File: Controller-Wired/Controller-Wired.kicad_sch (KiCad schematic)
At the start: 32 parts, among them J1 Conn_01x03, J2 Conn_02x20_Odd_Even, J3 Conn_01x06, J4 USB_C_Receptacle, SW1 SW_Push, U1 STM32F103CBTx, U2 AP131-33, U3 USBLC6-2SC6, Y1 Crystal

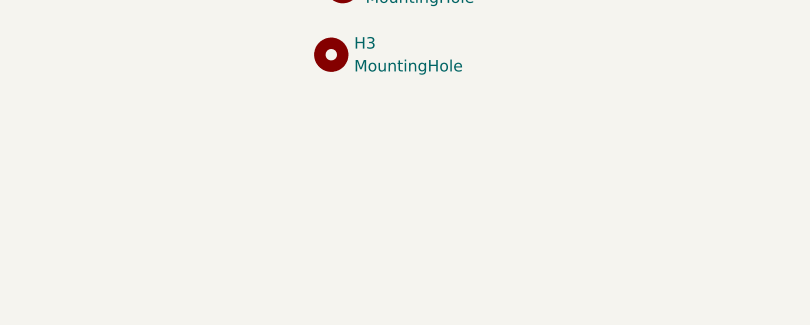
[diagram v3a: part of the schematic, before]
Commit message: Added an extra mounting hole to controller board       -I Noticed some import errors on the usb-c fp when I cloned this on my laptop, go back and review all pads before sending to JLC
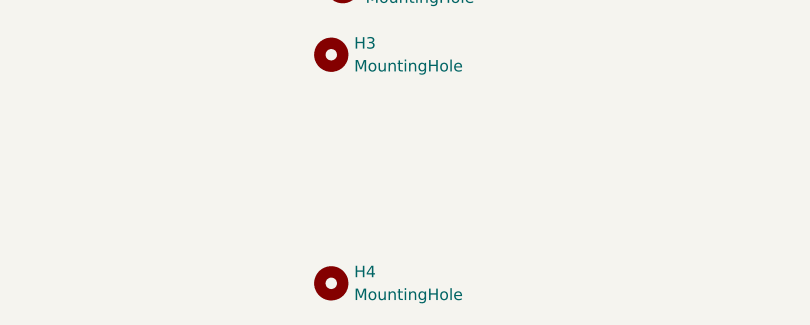
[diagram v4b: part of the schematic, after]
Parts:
- added H4: MountingHole, MountingHole:MountingHole_3.2mm_M3_Pad_Via, symbol Mechanical:MountingHole
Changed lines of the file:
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@@
+	)
+	(symbol
+		(lib_id "Mechanical:MountingHole")
+		(at 100.33 179.07 0)
+		(unit 1)
+		(exclude_from_sim no)
+		(in_bom no)
+		(on_board yes)
+		(dnp no)
+		(fields_autoplaced yes)
+		(property "Reference" "H4"
+			(at 102.87 177.7999 0)
+			(effects
+				(font
+					(size 1.27 1.27)
+				)
+				(justify left)
+			)
+		)
+		(property "Value" "MountingHole"
+			(at 102.87 180.3399 0)
+			(effects
+				(font
+					(size 1.27 1.27)
+				)
+				(justify left)
+			)
+		)
+		(property "Footprint" "MountingHole:MountingHole_3.2mm_M3_Pad_Via"
+			(at 100.33 179.07 0)
+			(effects
+				(font
+					(size 1.27 1.27)
+				)
+				(hide yes)
+			)
+		)
+		(property "Datasheet" "~"
+			(at 100.33 179.07 0)
+			(effects
+				(font
+					(size 1.27 1.27)
+				)
+				(hide yes)
+			)
+		)
+		(property "Description" "Mounting Hole without connection"
+			(at 100.33 179.07 0)
+			(effects
+				(font
+					(size 1.27 1.27)
+				)
+				(hide yes)
+			)
+		)
+		(instances
+			(project "Controller-Wired"
+				(path "/59e4fdea-365a-4456-b71a-51c7b872f1a3"
+					(reference "H4")
+					(unit 1)
+				)
+			)
+		)
 	)
 	(symbol

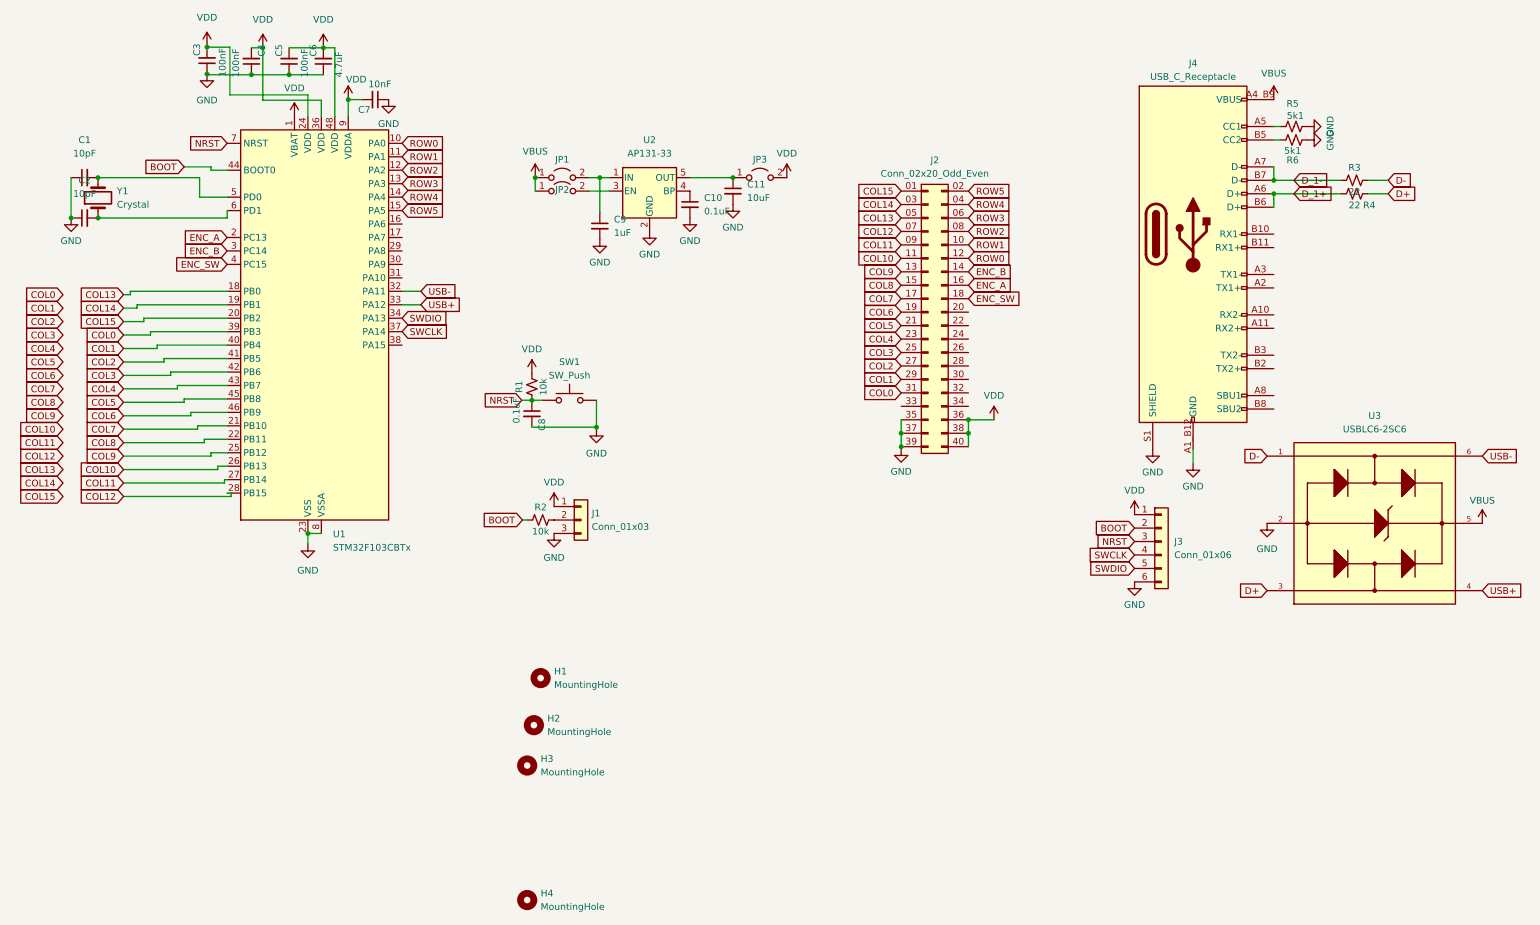
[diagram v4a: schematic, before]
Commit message: USB connector was giving some net problems, swapped with a different one
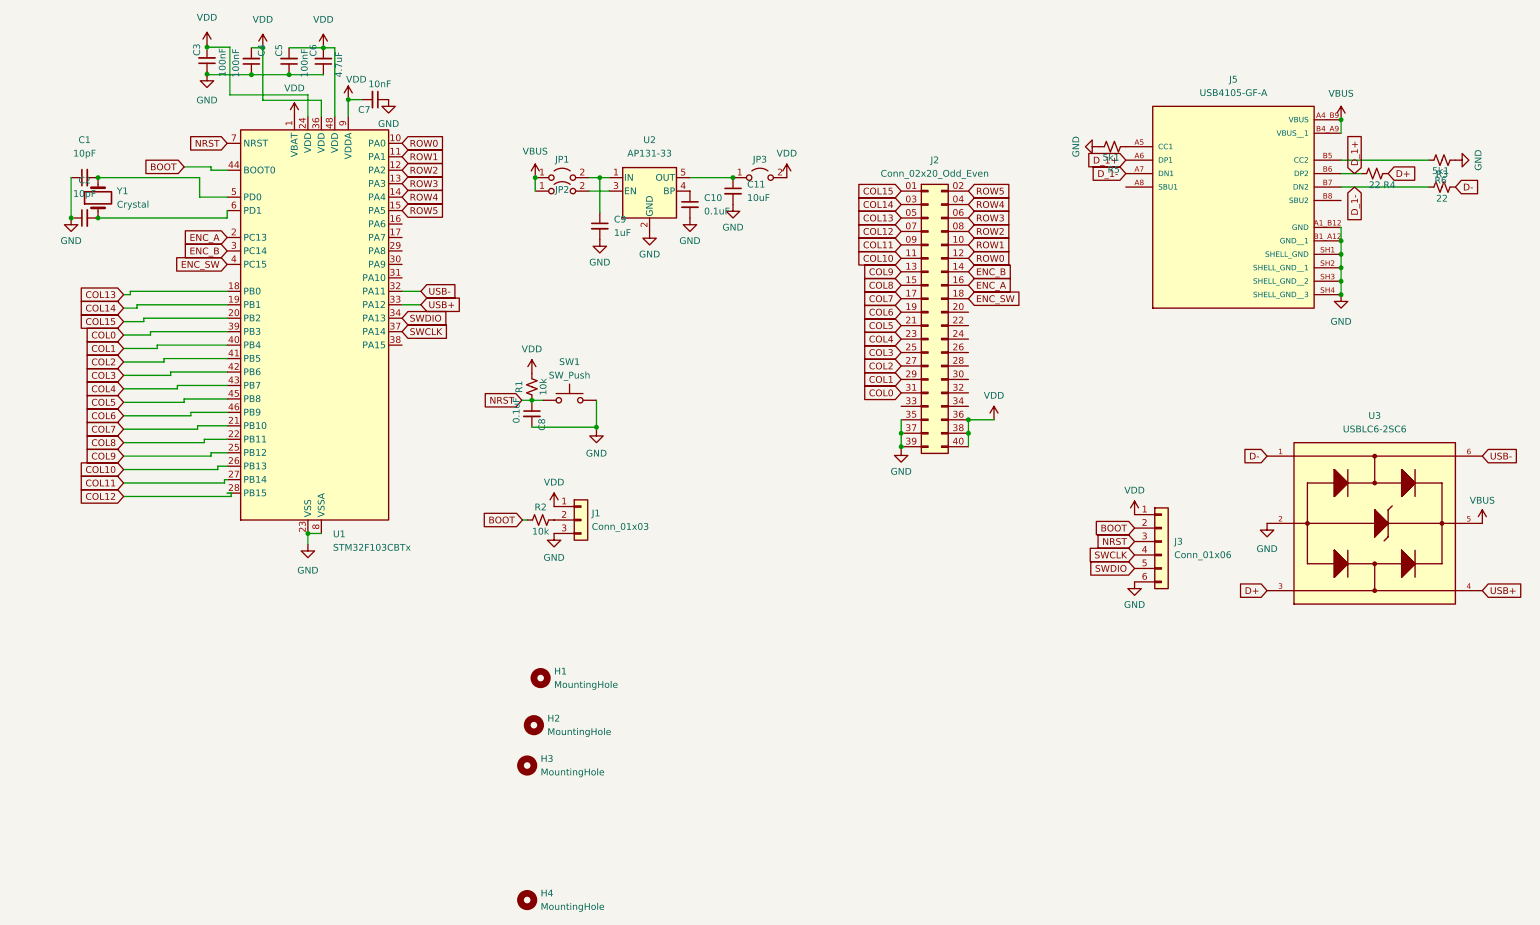
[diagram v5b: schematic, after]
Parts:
- removed J4: USB_C_Receptacle, Controller:AMPHENOL_12402012E212A, symbol Connector:USB_C_Receptacle
- added J5: USB4105-GF-A, Controller:GCT_USB4105-GF-A, symbol Keyboard:USB4105-GF-A
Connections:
- net D_1+: now also J5.A6 (DP1), J5.B6 (DP2)
- net D_1-: now also J5.A7 (DN1), J5.B7 (DN2)
- net GND: now also J5.A1_B12 (GND), J5.B1_A12 (GND__1), J5.SH1 (SHELL_GND), J5.SH2 (SHELL_GND__1), J5.SH3 (SHELL_GND__2), J5.SH4 (SHELL_GND__3)
- net VBUS: now also J5.A4_B9 (VBUS), J5.B4_A9 (VBUS__1)
- net at R5.1: now also J5.A5 (CC1)
- net at R6.2: now also J5.B5 (CC2)
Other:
- moved on the sheet: R3, R4, R5, R6
